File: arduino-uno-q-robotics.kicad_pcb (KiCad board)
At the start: 4 copper layers, 68.6 x 53.3 mm, 15 parts, among them J1 Conn_02x30_Odd_Even, J2 Conn_02x30_Odd_Even, J3 Connector_FFC-FPC, J5 Conn_02x30_Odd_Even, U1 LSM6DSO32, U2 TCA9803

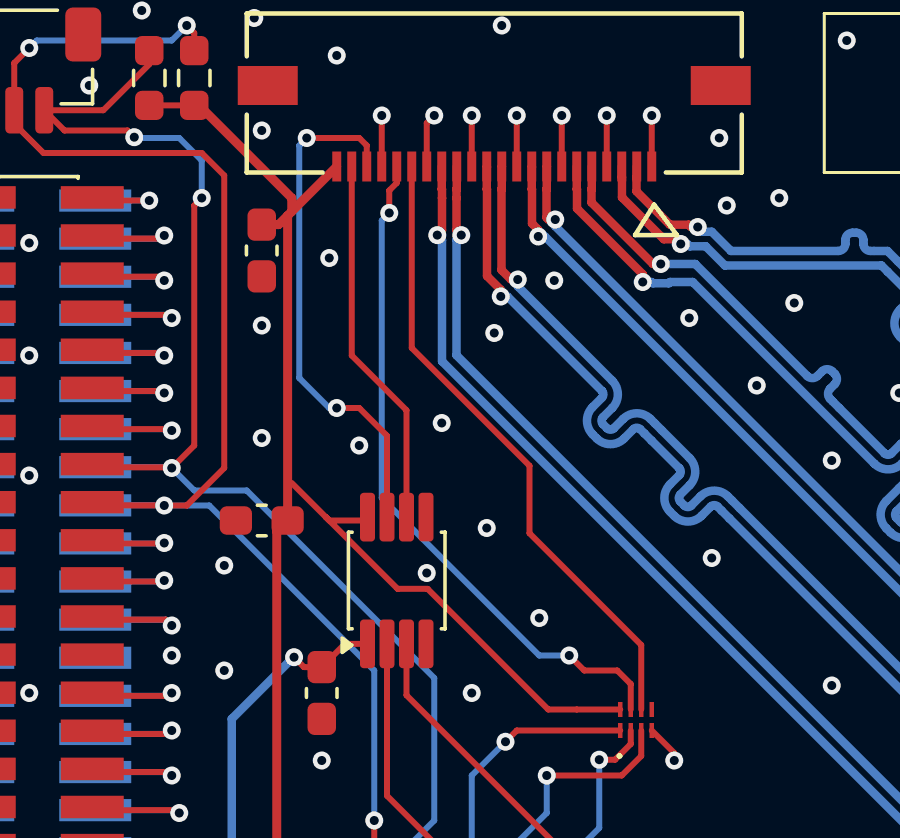
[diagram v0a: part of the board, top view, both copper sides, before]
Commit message: Adjust traces
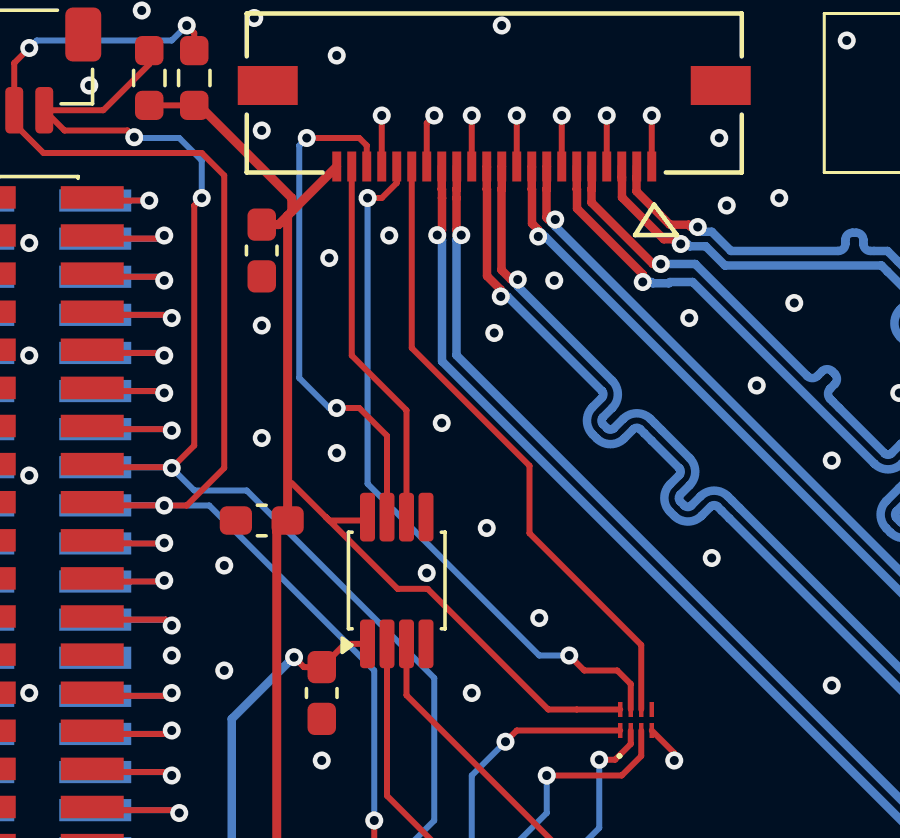
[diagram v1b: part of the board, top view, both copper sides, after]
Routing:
- net /SOC_CAM_MCLK0_3.3V: track 23.0 -> 23.6 mm
- net GND: vias 125 -> 126
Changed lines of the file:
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@@
 	)
 	(via
+		(at 138.25 76.25)
+		(size 0.6)
+		(drill 0.3)
+		(layers "F.Cu" "B.Cu")
+		(free yes)
+		(net 4)
+	)
+	(via
 		(at 132.75 90.75)
 		(size 0.6)
@@
 	)
 	(via
-		(at 137.25 83.25)
+		(at 136.5 83.5)
 		(size 0.6)
 		(drill 0.3)
@@
 	)
 	(segment
-		(start 144.25 90.25)
-		(end 144.75 90.75)
+		(start 138.499999 74.500001)
+		(end 138.499999 73.95)
 		(width 0.2)
 		(layer "F.Cu")
@@
 	)
 	(segment
-		(start 138.25 74.75)
-		(end 138.499999 74.500001)
+		(start 144.25 90.25)
+		(end 144.75 90.75)
 		(width 0.2)
 		(layer "F.Cu")
@@
 	)
 	(segment
-		(start 138.499999 74.500001)
-		(end 138.499999 73.95)
+		(start 138 75)
+		(end 138.499999 74.500001)
 		(width 0.2)
 		(layer "F.Cu")
@@
 	)
 	(segment
-		(start 138.25 75.5)
-		(end 138.25 74.75)
+		(start 137.527 75)
+		(end 138 75)
 		(width 0.2)
 		(layer "F.Cu")
@@
 	)
 	(via
-		(at 138.25 75.5)
+		(at 137.527 75)
 		(size 0.6)
 		(drill 0.3)
@@
 	)
 	(segment
-		(start 144.25 90.25)
+		(start 137.527 84.527)
 		(end 143.25 90.25)
 		(width 0.2)
@@
 	)
 	(segment
-		(start 138 75.75)
-		(end 138.25 75.5)
+		(start 137.527 75)
+		(end 137.527 84.527)
 		(width 0.2)
 		(layer "B.Cu")
@@
 	(segment
 		(start 143.25 90.25)
-		(end 138 85)
+		(end 144.25 90.25)
 		(width 0.2)
 		(layer "B.Cu")
@@
 	)
 	(segment
-		(start 138 85)
-		(end 138 75.75)
+		(start 142.925 83.925)
+		(end 139 80)
 		(width 0.2)
-		(layer "B.Cu")
-		(net 102)
+		(layer "F.Cu")
+		(net 104)
 	)
 	(segment
@@
 		(width 0.2)
 		(layer "F.Cu")
-		(net 104)
-	)
-	(segment
-		(start 142.925 83.925)
-		(end 139 80)
-		(width 0.2)
-		(layer "F.Cu")
